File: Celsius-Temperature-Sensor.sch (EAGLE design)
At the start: 18 parts, among them Q1 BSS138, Q2 BSS138

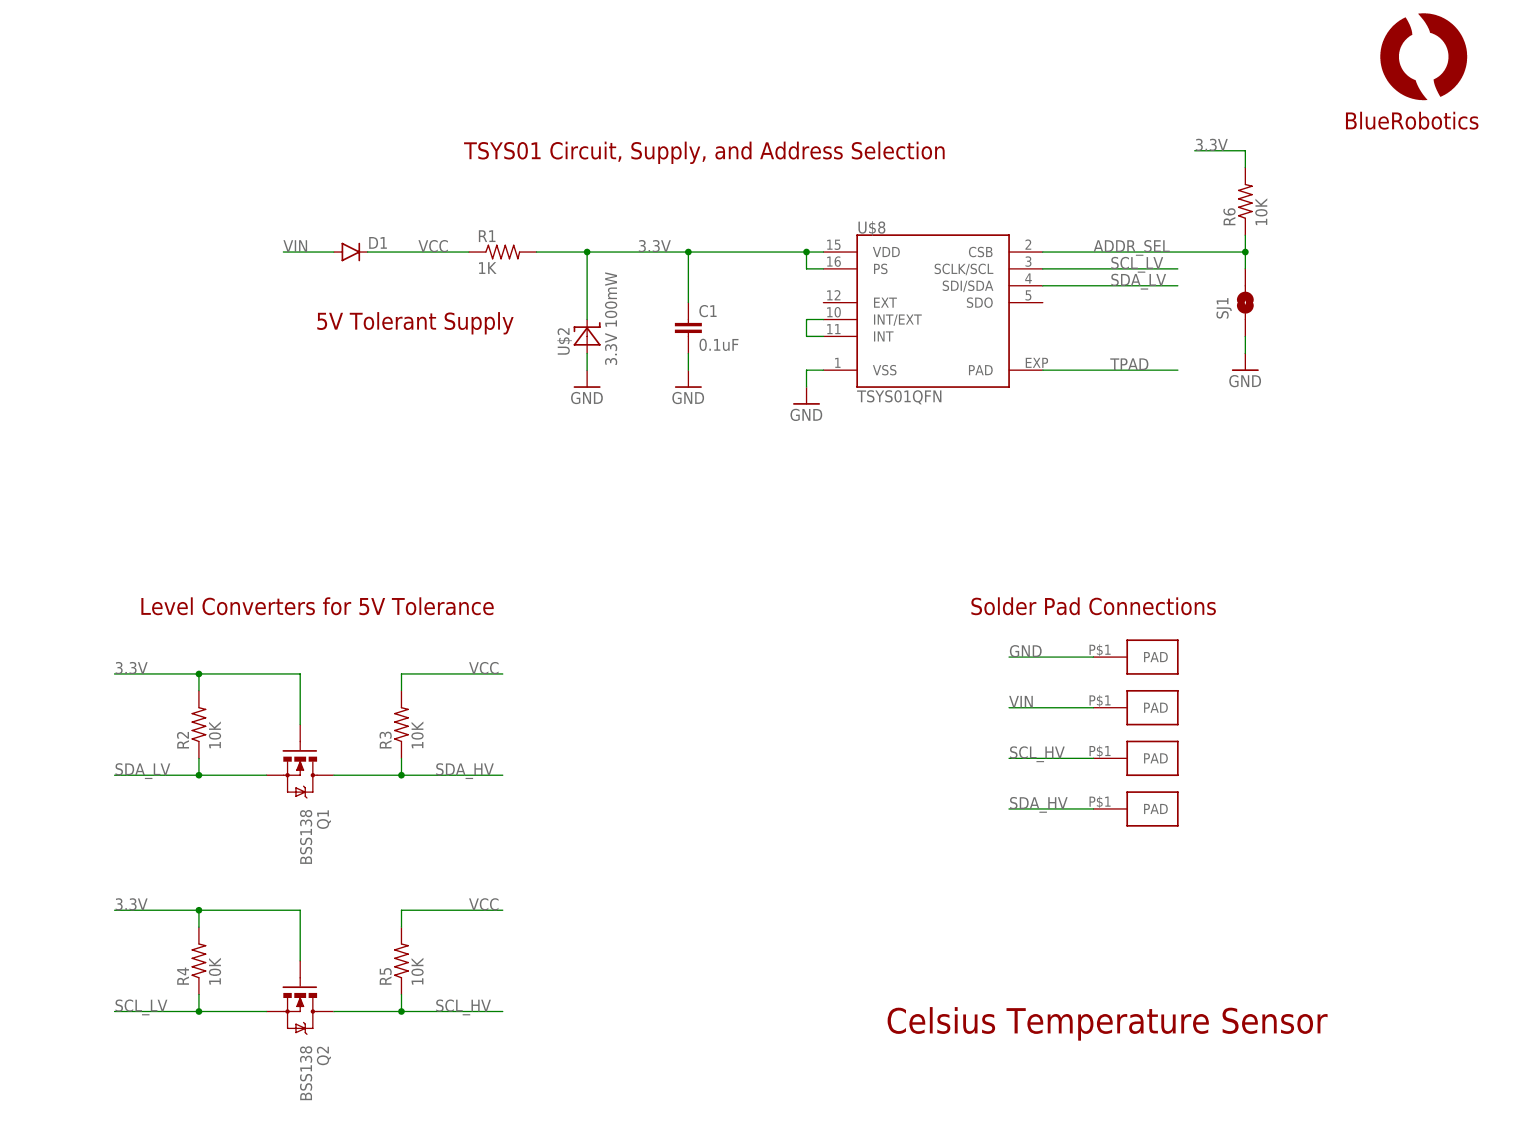
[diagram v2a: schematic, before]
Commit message: Updated zener to LDO.
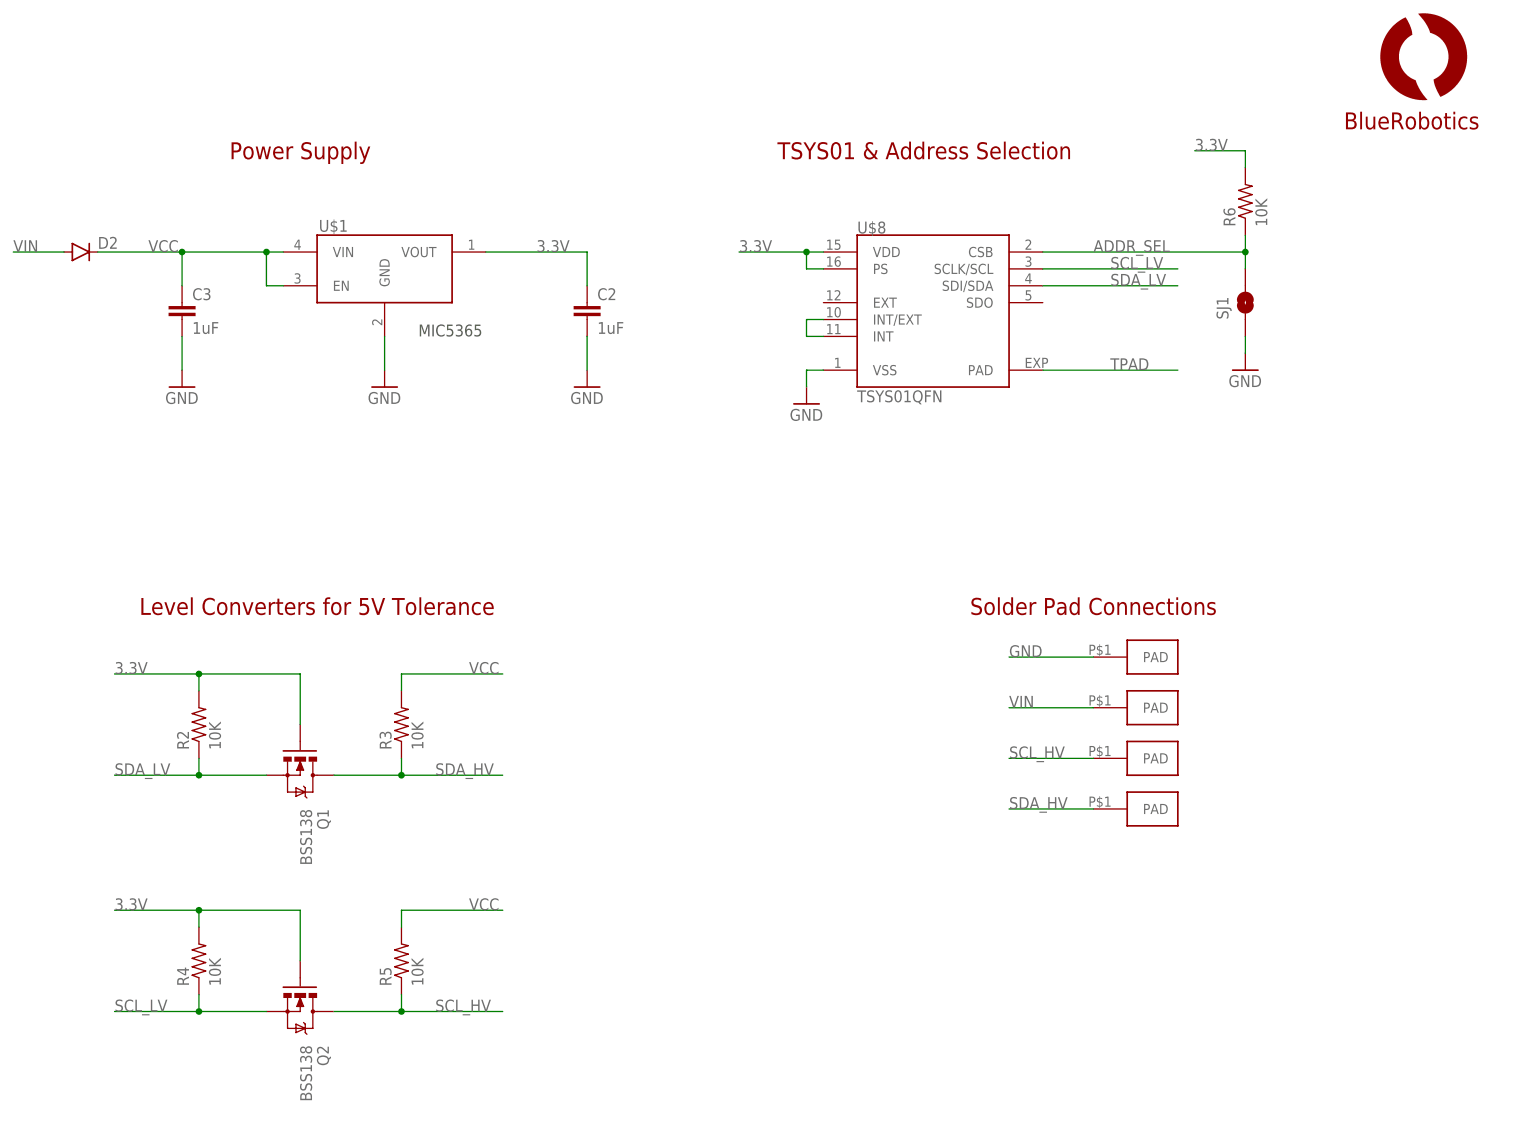
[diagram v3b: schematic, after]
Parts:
- removed C1: 0.1uF, resistor:C-EUC0402
- removed D1: (no value), SparkFun-DiscreteSemi:DIODESOD523
- removed R1: 1K, resistor:R-US_R0402
- removed U$2: 3.3V 100mW, BR-Eagle-Library:DIODE-ZENER0603/SOD-523
- added C2, C3: 1uF, resistor:C-EUC0402
- added D2: (no value), SparkFun-DiscreteSemi:DIODESOD523
- added U$1: VREG-MIC5365, BlueRobotics-Main:VREG-MIC5365
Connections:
- net 3.3V: now also C2.1, U$1.VOUT; no longer C1.1, R1.2, U$2.C
- net GND: now also C2.2, C3.2, U$1.GND; no longer C1.2, U$2.A
- net VCC: now also C3.1, D2.C, U$1.EN, U$1.VIN; no longer D1.C, R1.1
- net VIN: now also D2.A; no longer D1.A
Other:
- note added: "MIC5365"
- note added: "Power Supply"
- note added: "TSYS01 & Address Selection"
- note removed: "5V Tolerant Supply"
- note removed: "Celsius Temperature Sensor"
- note removed: "TSYS01 Circuit, Supply, and Address Selection"
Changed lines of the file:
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@@
 </classes>
 <parts>
-<part name="C1" library="resistor" deviceset="C-EU" device="C0402" value="0.1uF"/>
-<part name="R1" library="resistor" deviceset="R-US_" device="R0402" value="1K"/>
-<part name="U$2" library="BR-Eagle-Library" deviceset="DIODE-ZENER" device="0603/SOD-523" value="3.3V 100mW"/>
-<part name="GND1" library="supply1" deviceset="GND" device=""/>
-<part name="GND2" library="supply1" deviceset="GND" device=""/>
 <part name="GND3" library="supply1" deviceset="GND" device=""/>
 <part name="Q1" library="SparkFun-DiscreteSemi" deviceset="MOSFET-NCHANNEL" device="2N7002PW" value="BSS138"/>
@@
 <part name="R4" library="resistor" deviceset="R-US_" device="R0402" value="10K"/>
 <part name="R5" library="resistor" deviceset="R-US_" device="R0402" value="10K"/>
-<part name="D1" library="SparkFun-DiscreteSemi" deviceset="DIODE" device="SOD523"/>
 <part name="U$3" library="BR-Eagle-Library" deviceset="PAD" device="1.5X3MM"/>
 <part name="U$4" library="BR-Eagle-Library" deviceset="PAD" device="1.5X3MM"/>
@@
 <part name="GND4" library="supply1" deviceset="GND" device=""/>
 <part name="R6" library="resistor" deviceset="R-US_" device="R0402" value="10K"/>
+<part name="C2" library="resistor" deviceset="C-EU" device="C0402" value="1uF"/>
+<part name="GND5" library="supply1" deviceset="GND" device=""/>
+<part name="GND6" library="supply1" deviceset="GND" device=""/>
+<part name="D2" library="SparkFun-DiscreteSemi" deviceset="DIODE" device="SOD523"/>
+<part name="U$1" library="BlueRobotics-Main" deviceset="VREG-MIC5365" device=""/>
+<part name="C3" library="resistor" deviceset="C-EU" device="C0402" value="1uF"/>
+<part name="GND7" library="supply1" deviceset="GND" device=""/>
 </parts>
 <sheets>
 <sheet>
 <plain>
-<text x="52.578" y="-61.722" size="3.81" layer="94">Celsius Temperature Sensor</text>
 <text x="-33.02" y="2.54" size="2.54" layer="94" align="center">Level Converters for 5V Tolerance</text>
-<text x="-18.288" y="45.466" size="2.54" layer="94" align="center">5V Tolerant Supply</text>
 <text x="83.82" y="2.54" size="2.54" layer="94" align="center">Solder Pad Connections</text>
-<text x="25.4" y="71.12" size="2.54" layer="94" align="center">TSYS01 Circuit, Supply, and Address Selection</text>
+<text x="58.42" y="71.12" size="2.54" layer="94" align="center">TSYS01 &amp; Address Selection</text>
+<text x="-35.56" y="71.12" size="2.54" layer="94" align="center">Power Supply</text>
+<text x="-17.78" y="43.18" size="1.778" layer="97">MIC5365</text>
 </plain>
 <instances>
-<instance part="C1" gate="G$1" x="22.86" y="45.72"/>
-<instance part="R1" gate="G$1" x="-5.08" y="55.88"/>
-<instance part="U$2" gate="G$1" x="7.62" y="43.18" rot="R90"/>
-<instance part="GND1" gate="1" x="7.62" y="35.56"/>
-<instance part="GND2" gate="1" x="22.86" y="35.56"/>
 <instance part="GND3" gate="1" x="40.64" y="33.02"/>
 <instance part="Q1" gate="G$1" x="-35.56" y="-22.86" rot="R270"/>
@@
 <instance part="R4" gate="G$1" x="-50.8" y="-50.8" rot="R90"/>
 <instance part="R5" gate="G$1" x="-20.32" y="-50.8" rot="R90"/>
-<instance part="D1" gate="G$1" x="-27.94" y="55.88"/>
 <instance part="U$3" gate="G$1" x="88.9" y="-5.08"/>
 <instance part="U$4" gate="G$1" x="88.9" y="-12.7"/>
@@
 <instance part="GND4" gate="1" x="106.68" y="38.1"/>
 <instance part="R6" gate="G$1" x="106.68" y="63.5" rot="R90"/>
+<instance part="C2" gate="G$1" x="7.62" y="48.26"/>
+<instance part="GND5" gate="1" x="-22.86" y="35.56"/>
+<instance part="GND6" gate="1" x="7.62" y="35.56"/>
+<instance part="D2" gate="G$1" x="-68.58" y="55.88"/>
+<instance part="U$1" gate="G$1" x="-33.02" y="50.8"/>
+<instance part="C3" gate="G$1" x="-53.34" y="48.26"/>
+<instance part="GND7" gate="1" x="-53.34" y="35.56"/>
 </instances>
 <busses>
@@
 <net name="GND" class="0">
 <segment>
-<pinref part="GND1" gate="1" pin="GND"/>
-<pinref part="U$2" gate="G$1" pin="A"/>
-<wire x1="7.62" y1="38.1" x2="7.62" y2="40.64" width="0.1524" layer="91"/>
-</segment>
-<segment>
-<pinref part="C1" gate="G$1" pin="2"/>
-<pinref part="GND2" gate="1" pin="GND"/>
-<wire x1="22.86" y1="40.64" x2="22.86" y2="38.1" width="0.1524" layer="91"/>
-</segment>
-<segment>
 <wire x1="83.82" y1="-5.08" x2="71.12" y2="-5.08" width="0.1524" layer="91"/>
 <label x="71.12" y="-5.08" size="1.778" layer="95"/>
@@
 <pinref part="SJ1" gate="G$1" pin="1"/>
 <wire x1="106.68" y1="40.64" x2="106.68" y2="43.18" width="0.1524" layer="91"/>
+</segment>
+<segment>
+<pinref part="C2" gate="G$1" pin="2"/>
+<pinref part="GND6" gate="1" pin="GND"/>
+<wire x1="7.62" y1="43.18" x2="7.62" y2="38.1" width="0.1524" layer="91"/>
+</segment>
+<segment>
+<pinref part="GND5" gate="1" pin="GND"/>
+<pinref part="U$1" gate="G$1" pin="GND"/>
+<wire x1="-22.86" y1="38.1" x2="-22.86" y2="43.18" width="0.1524" layer="91"/>
+</segment>
+<segment>
+<pinref part="C3" gate="G$1" pin="2"/>
+<pinref part="GND7" gate="1" pin="GND"/>
+<wire x1="-53.34" y1="38.1" x2="-53.34" y2="43.18" width="0.1524" layer="91"/>
 </segment>
 </net>
@@
 </segment>
 <segment>
-<pinref part="R1" gate="G$1" pin="2"/>
 <wire x1="43.18" y1="55.88" x2="40.64" y2="55.88" width="0.1524" layer="91"/>
-<pinref part="U$2" gate="G$1" pin="C"/>
-<wire x1="40.64" y1="55.88" x2="22.86" y2="55.88" width="0.1524" layer="91"/>
-<wire x1="22.86" y1="55.88" x2="7.62" y2="55.88" width="0.1524" layer="91"/>
-<wire x1="7.62" y1="55.88" x2="0" y2="55.88" width="0.1524" layer="91"/>
-<wire x1="7.62" y1="45.72" x2="7.62" y2="55.88" width="0.1524" layer="91"/>
-<junction x="7.62" y="55.88"/>
-<pinref part="C1" gate="G$1" pin="1"/>
-<wire x1="22.86" y1="48.26" x2="22.86" y2="55.88" width="0.1524" layer="91"/>
-<junction x="22.86" y="55.88"/>
-<label x="15.24" y="55.88" size="1.778" layer="95"/>
+<wire x1="40.64" y1="55.88" x2="30.48" y2="55.88" width="0.1524" layer="91"/>
+<label x="30.48" y="55.88" size="1.778" layer="95"/>
 <pinref part="U$8" gate="G$1" pin="VDD"/>
 <pinref part="U$8" gate="G$1" pin="PS"/>
@@
 <label x="99.06" y="71.12" size="1.778" layer="95"/>
 </segment>
+<segment>
+<wire x1="7.62" y1="55.88" x2="-7.62" y2="55.88" width="0.1524" layer="91"/>
+<pinref part="C2" gate="G$1" pin="1"/>
+<wire x1="7.62" y1="50.8" x2="7.62" y2="55.88" width="0.1524" layer="91"/>
+<label x="0" y="55.88" size="1.778" layer="95"/>
+<pinref part="U$1" gate="G$1" pin="VOUT"/>
+</segment>
 </net>
 <net name="VCC" class="0">
@@
 </segment>
 <segment>
-<pinref part="R1" gate="G$1" pin="1"/>
-<wire x1="-10.16" y1="55.88" x2="-25.4" y2="55.88" width="0.1524" layer="91"/>
-<label x="-17.78" y="55.88" size="1.778" layer="95"/>
-<pinref part="D1" gate="G$1" pin="C"/>
+<wire x1="-38.1" y1="55.88" x2="-40.64" y2="55.88" width="0.1524" layer="91"/>
+<label x="-58.42" y="55.88" size="1.778" layer="95"/>
+<pinref part="D2" gate="G$1" pin="C"/>
+<pinref part="U$1" gate="G$1" pin="VIN"/>
+<pinref part="U$1" gate="G$1" pin="EN"/>
+<wire x1="-40.64" y1="55.88" x2="-53.34" y2="55.88" width="0.1524" layer="91"/>
+<wire x1="-53.34" y1="55.88" x2="-66.04" y2="55.88" width="0.1524" layer="91"/>
+<wire x1="-38.1" y1="50.8" x2="-40.64" y2="50.8" width="0.1524" layer="91"/>
+<wire x1="-40.64" y1="50.8" x2="-40.64" y2="55.88" width="0.1524" layer="91"/>
+<junction x="-40.64" y="55.88"/>
+<pinref part="C3" gate="G$1" pin="1"/>
+<wire x1="-53.34" y1="50.8" x2="-53.34" y2="55.88" width="0.1524" layer="91"/>
+<junction x="-53.34" y="55.88"/>
 </segment>
 </net>
@@
 <net name="VIN" class="0">
 <segment>
-<pinref part="D1" gate="G$1" pin="A"/>
-<wire x1="-30.48" y1="55.88" x2="-38.1" y2="55.88" width="0.1524" layer="91"/>
-<label x="-38.1" y="55.88" size="1.778" layer="95"/>
-</segment>
-<segment>
 <wire x1="83.82" y1="-12.7" x2="71.12" y2="-12.7" width="0.1524" layer="91"/>
 <label x="71.12" y="-12.7" size="1.778" layer="95"/>
 <pinref part="U$4" gate="G$1" pin="PAD"/>
 </segment>
-</net>
+<segment>
+<pinref part="D2" gate="G$1" pin="A"/>
+<wire x1="-71.12" y1="55.88" x2="-78.74" y2="55.88" width="0.1524" layer="91"/>
+<label x="-78.74" y="55.88" size="1.778" layer="95"/>
+</segment>
+</net>

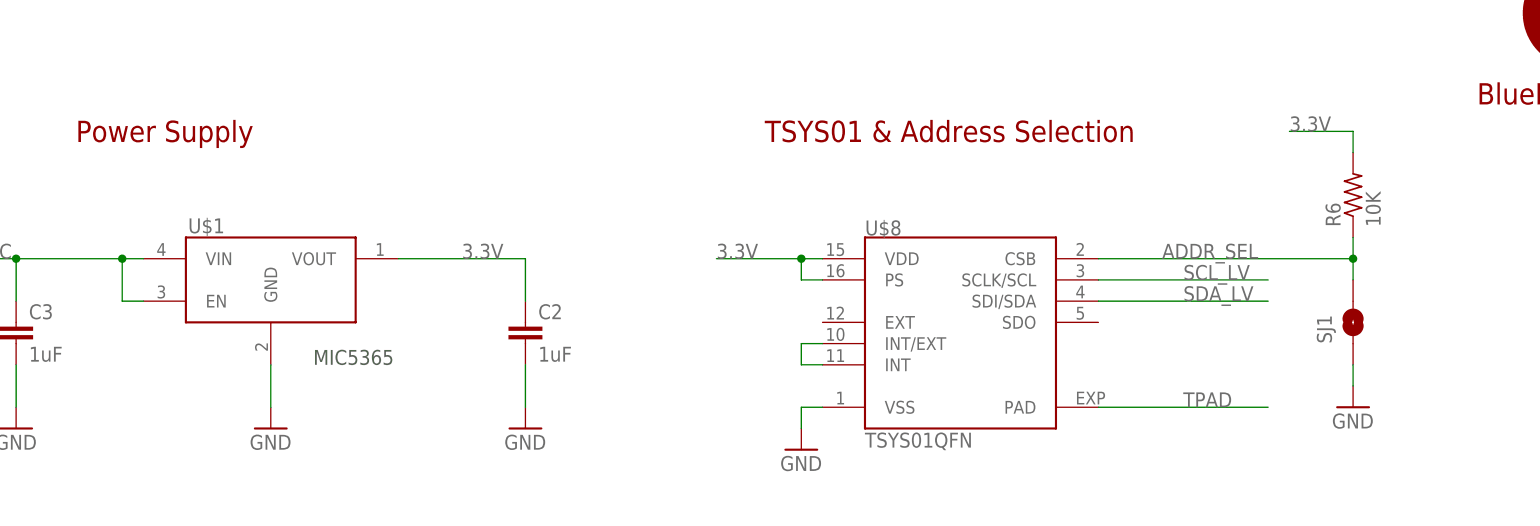
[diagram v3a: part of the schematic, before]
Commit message: Fixed incorrect regulator footprint. Stupid mistake.
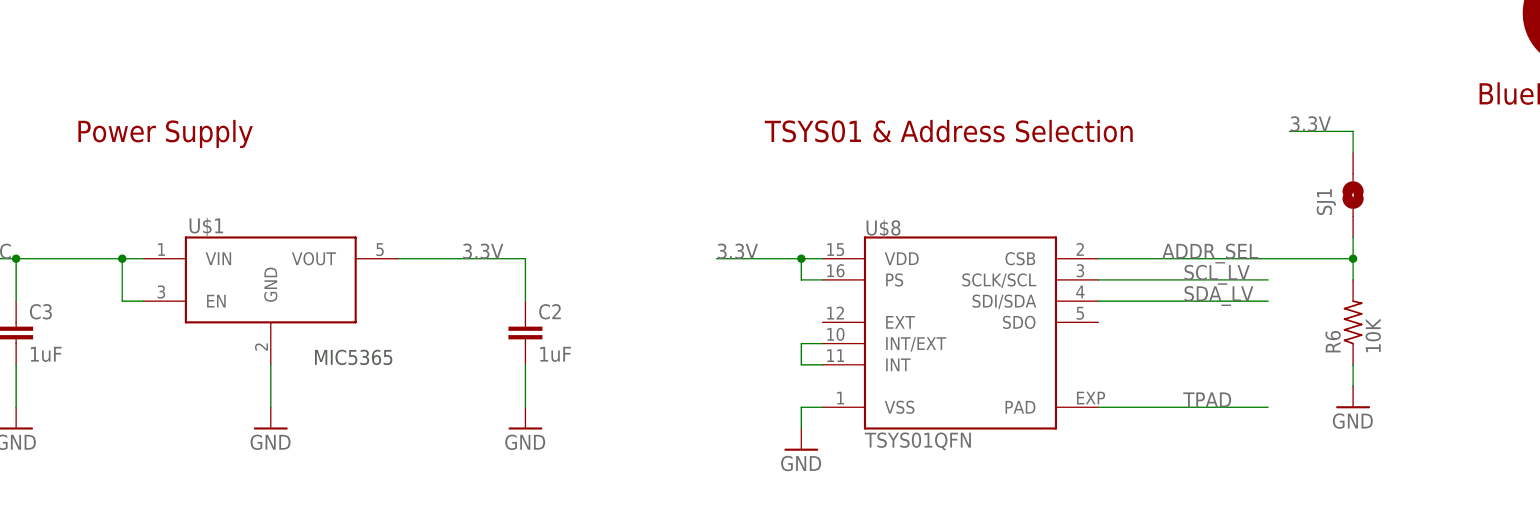
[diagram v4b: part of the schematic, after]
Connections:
- net 3.3V: now also SJ1.2; no longer R6.2
- net ADDR_SEL: now also R6.2, SJ1.1; no longer R6.1, SJ1.2
- net GND: now also R6.1; no longer SJ1.1
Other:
- moved on the sheet: R6, SJ1
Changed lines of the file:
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@@
 <instance part="U$7" gate="G$1" x="127" y="78.74"/>
 <instance part="U$8" gate="G$1" x="48.26" y="35.56"/>
-<instance part="SJ1" gate="G$1" x="106.68" y="48.26" smashed="yes" rot="R90">
-<attribute name="NAME" x="104.14" y="45.72" size="1.778" layer="95" rot="R90"/>
+<instance part="SJ1" gate="G$1" x="106.68" y="63.5" smashed="yes" rot="R90">
+<attribute name="NAME" x="104.14" y="60.96" size="1.778" layer="95" rot="R90"/>
 </instance>
 <instance part="GND4" gate="1" x="106.68" y="38.1"/>
-<instance part="R6" gate="G$1" x="106.68" y="63.5" rot="R90"/>
+<instance part="R6" gate="G$1" x="106.68" y="48.26" rot="R90"/>
 <instance part="C2" gate="G$1" x="7.62" y="48.26"/>
 <instance part="GND5" gate="1" x="-22.86" y="35.56"/>
@@
 </segment>
 <segment>
-<pinref part="GND4" gate="1" pin="GND"/>
-<pinref part="SJ1" gate="G$1" pin="1"/>
-<wire x1="106.68" y1="40.64" x2="106.68" y2="43.18" width="0.1524" layer="91"/>
-</segment>
-<segment>
 <pinref part="C2" gate="G$1" pin="2"/>
 <pinref part="GND6" gate="1" pin="GND"/>
@@
 <pinref part="GND7" gate="1" pin="GND"/>
 <wire x1="-53.34" y1="38.1" x2="-53.34" y2="43.18" width="0.1524" layer="91"/>
+</segment>
+<segment>
+<pinref part="GND4" gate="1" pin="GND"/>
+<pinref part="R6" gate="G$1" pin="1"/>
+<wire x1="106.68" y1="40.64" x2="106.68" y2="43.18" width="0.1524" layer="91"/>
 </segment>
 </net>
@@
 </segment>
 <segment>
-<pinref part="R6" gate="G$1" pin="2"/>
-<wire x1="106.68" y1="68.58" x2="106.68" y2="71.12" width="0.1524" layer="91"/>
 <wire x1="106.68" y1="71.12" x2="99.06" y2="71.12" width="0.1524" layer="91"/>
 <label x="99.06" y="71.12" size="1.778" layer="95"/>
+<pinref part="SJ1" gate="G$1" pin="2"/>
+<wire x1="106.68" y1="68.58" x2="106.68" y2="71.12" width="0.1524" layer="91"/>
 </segment>
 <segment>
@@
 <wire x1="76.2" y1="55.88" x2="106.68" y2="55.88" width="0.1524" layer="91"/>
 <label x="83.82" y="55.88" size="1.778" layer="95"/>
-<pinref part="SJ1" gate="G$1" pin="2"/>
-<pinref part="R6" gate="G$1" pin="1"/>
+<pinref part="R6" gate="G$1" pin="2"/>
 <wire x1="106.68" y1="53.34" x2="106.68" y2="55.88" width="0.1524" layer="91"/>
+<pinref part="SJ1" gate="G$1" pin="1"/>
 <wire x1="106.68" y1="55.88" x2="106.68" y2="58.42" width="0.1524" layer="91"/>
 <junction x="106.68" y="55.88"/>
